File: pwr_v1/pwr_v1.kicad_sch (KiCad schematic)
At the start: 2 parts

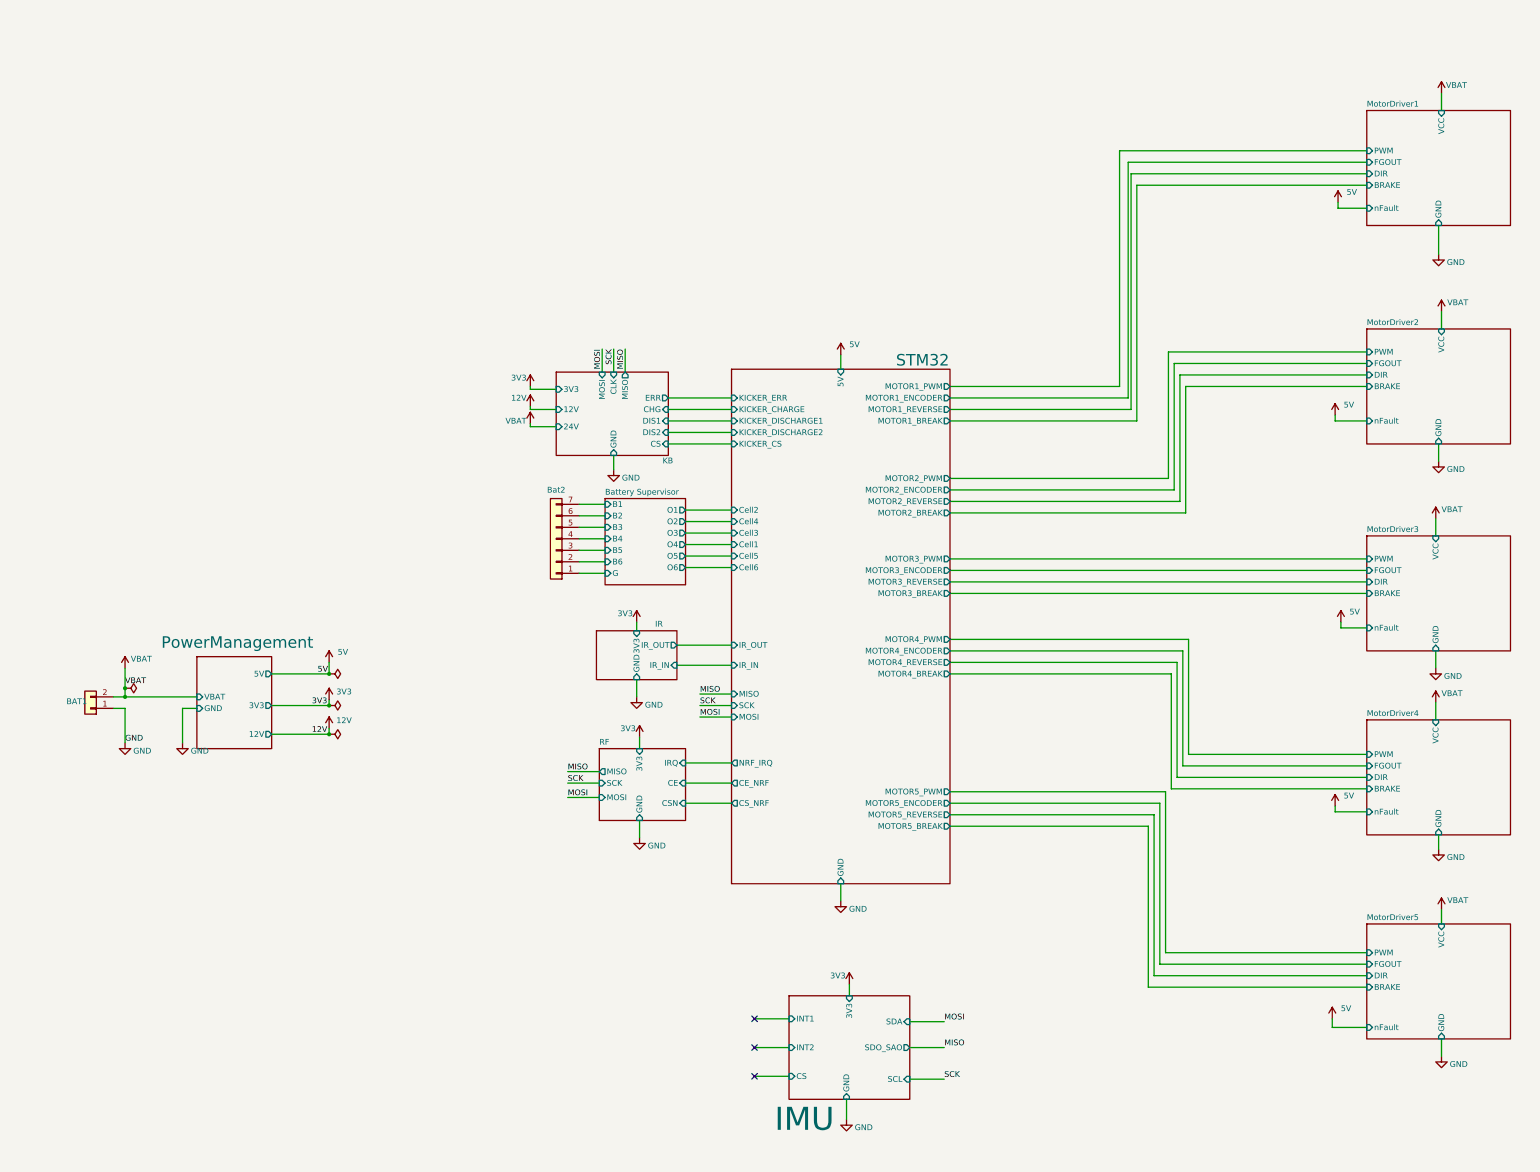
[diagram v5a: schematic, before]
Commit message: Schematic and layout updated; Layout placement and routing completed
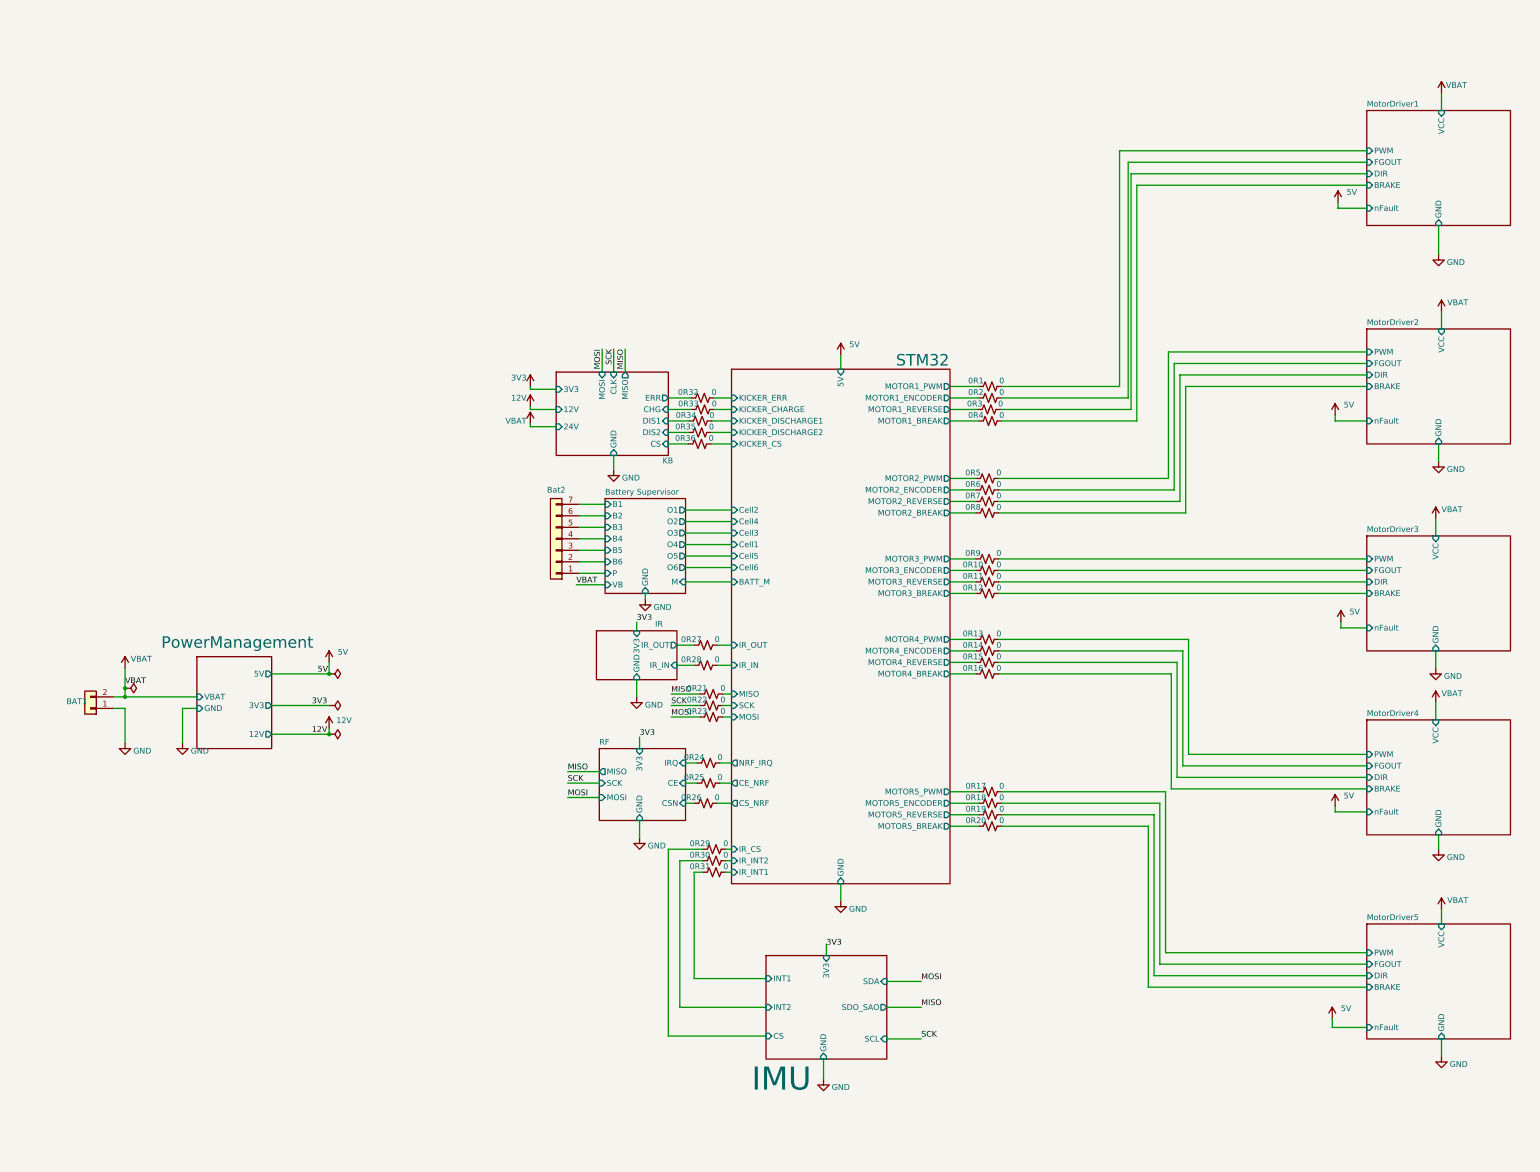
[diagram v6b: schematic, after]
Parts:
- added 0R1, 0R10, 0R11, 0R12, 0R13, 0R14, 0R15, 0R16, 0R17, 0R18, 0R19, 0R2, 0R20, 0R21, 0R22, 0R23, 0R24, 0R25, 0R26, 0R27, 0R28, 0R29, 0R3, 0R30, 0R31, 0R32, 0R33, 0R34, 0R35, 0R36, 0R4, 0R5, 0R6, 0R7, 0R8, 0R9: 0, Resistor_SMD:R_0603_1608Metric, symbol Device:R_Small_US
- Bat2: footprint (none) -> B7B_XH_A:JST_B7B-XH-A
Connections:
- net IMU/CS: now also 0R29.1
- net IMU/INT1: now also 0R31.1
- net IMU/INT2: now also 0R30.1
- net IR/IR_IN: now also 0R28.1
- net IR/IR_OUT: now also 0R27.1
- net KB/CHG: now also 0R33.1
- net KB/CS: now also 0R36.1
- net KB/DIS1: now also 0R34.1
- net KB/DIS2: now also 0R35.1
- net KB/ERR: now also 0R32.1
- net MISO: now also 0R21.1
- net MOSI: now also 0R23.1
- net MotorDriver1/BRAKE: now also 0R4.2
- net MotorDriver1/DIR: now also 0R3.2
- net MotorDriver1/FGOUT: now also 0R2.2
- net MotorDriver1/PWM: now also 0R1.2
- net MotorDriver2/BRAKE: now also 0R8.2
- net MotorDriver2/DIR: now also 0R7.2
- net MotorDriver2/FGOUT: now also 0R6.2
- net MotorDriver2/PWM: now also 0R5.2
- net MotorDriver3/BRAKE: now also 0R12.2
- net MotorDriver3/DIR: now also 0R11.2
- net MotorDriver3/FGOUT: now also 0R10.2
- net MotorDriver3/PWM: now also 0R9.2
- net MotorDriver4/BRAKE: now also 0R16.2
- net MotorDriver4/DIR: now also 0R15.2
- net MotorDriver4/FGOUT: now also 0R14.2
- net MotorDriver4/PWM: now also 0R13.2
- net MotorDriver5/BRAKE: now also 0R20.2
- net MotorDriver5/DIR: now also 0R19.2
- net MotorDriver5/FGOUT: now also 0R18.2
- net MotorDriver5/PWM: now also 0R17.2
- net RF/CE: now also 0R25.1
- net RF/CSN: now also 0R26.1
- net RF/IRQ: now also 0R24.1
- net SCK: now also 0R22.1
- net Battery Supervisor/G renamed Battery Supervisor/P
- new net STM32/CE_NRF: 0R25.2
- new net STM32/CS_NRF: 0R26.2
- new net STM32/IR_CS: 0R29.2
- new net STM32/IR_IN: 0R28.2
- new net STM32/IR_INT1: 0R31.2
- new net STM32/IR_INT2: 0R30.2
- new net STM32/IR_OUT: 0R27.2
- new net STM32/KICKER_CHARGE: 0R33.2
- new net STM32/KICKER_CS: 0R36.2
- new net STM32/KICKER_DISCHARGE1: 0R34.2
- new net STM32/KICKER_DISCHARGE2: 0R35.2
- new net STM32/KICKER_ERR: 0R32.2
- new net STM32/MISO: 0R21.2
- new net STM32/MOSI: 0R23.2
- new net STM32/MOTOR1_BREAK: 0R4.1
- new net STM32/MOTOR1_ENCODER: 0R2.1
- new net STM32/MOTOR1_PWM: 0R1.1
- new net STM32/MOTOR1_REVERSE: 0R3.1
- new net STM32/MOTOR2_BREAK: 0R8.1
- new net STM32/MOTOR2_ENCODER: 0R6.1
- new net STM32/MOTOR2_PWM: 0R5.1
- new net STM32/MOTOR2_REVERSE: 0R7.1
- new net STM32/MOTOR3_BREAK: 0R12.1
- new net STM32/MOTOR3_ENCODER: 0R10.1
- new net STM32/MOTOR3_PWM: 0R9.1
- new net STM32/MOTOR3_REVERSE: 0R11.1
- new net STM32/MOTOR4_BREAK: 0R16.1
- new net STM32/MOTOR4_ENCODER: 0R14.1
- new net STM32/MOTOR4_PWM: 0R13.1
- new net STM32/MOTOR4_REVERSE: 0R15.1
- new net STM32/MOTOR5_BREAK: 0R20.1
- new net STM32/MOTOR5_ENCODER: 0R18.1
- new net STM32/MOTOR5_PWM: 0R17.1
- new net STM32/MOTOR5_REVERSE: 0R19.1
- new net STM32/NRF_IRQ: 0R24.2
- new net STM32/SCK: 0R22.2
- no-connect marks 3 -> 0
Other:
- sheet Battery Supervisor ports: added GND, M, P, VB; removed G
- sheet STM32 ports: added BATT_M, IR_CS, IR_INT1, IR_INT2; removed none

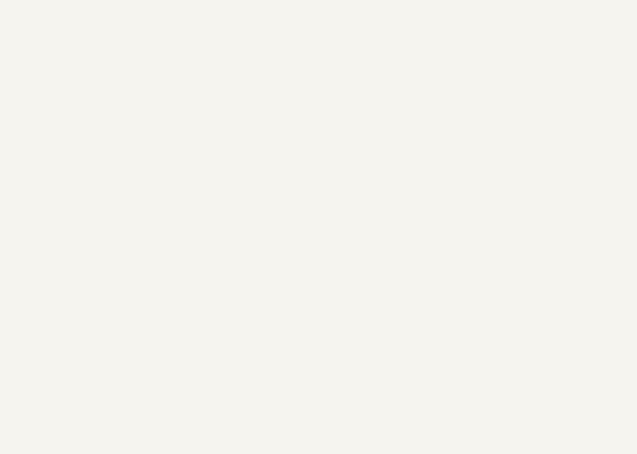
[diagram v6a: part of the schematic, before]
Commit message: Sch: Mechanical comp added; Lay: SIlkscreen aligned, trace widths updated to atleast 12 mils.
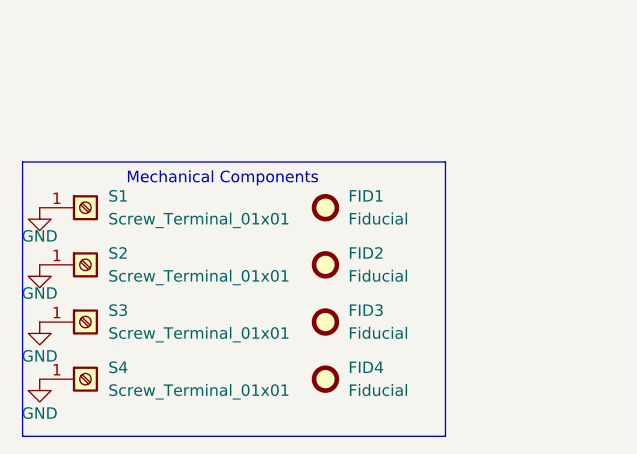
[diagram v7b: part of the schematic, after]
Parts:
- added FID1, FID2, FID3, FID4: Fiducial, Fiducial:Fiducial_1mm_Mask2mm, symbol Mechanical:Fiducial
- added S1, S2, S3, S4: Screw_Terminal_01x01, TerminalBlock_MetzConnect:TerminalBlock_MetzConnect_360271_1x01_Horizontal_ScrewM3.0_Boxed, symbol Connector:Screw_Terminal_01x01
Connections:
- net GND: now also S1.1 (Pin_1), S2.1 (Pin_1), S3.1 (Pin_1), S4.1 (Pin_1)
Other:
- note added: "Mechanical Components"

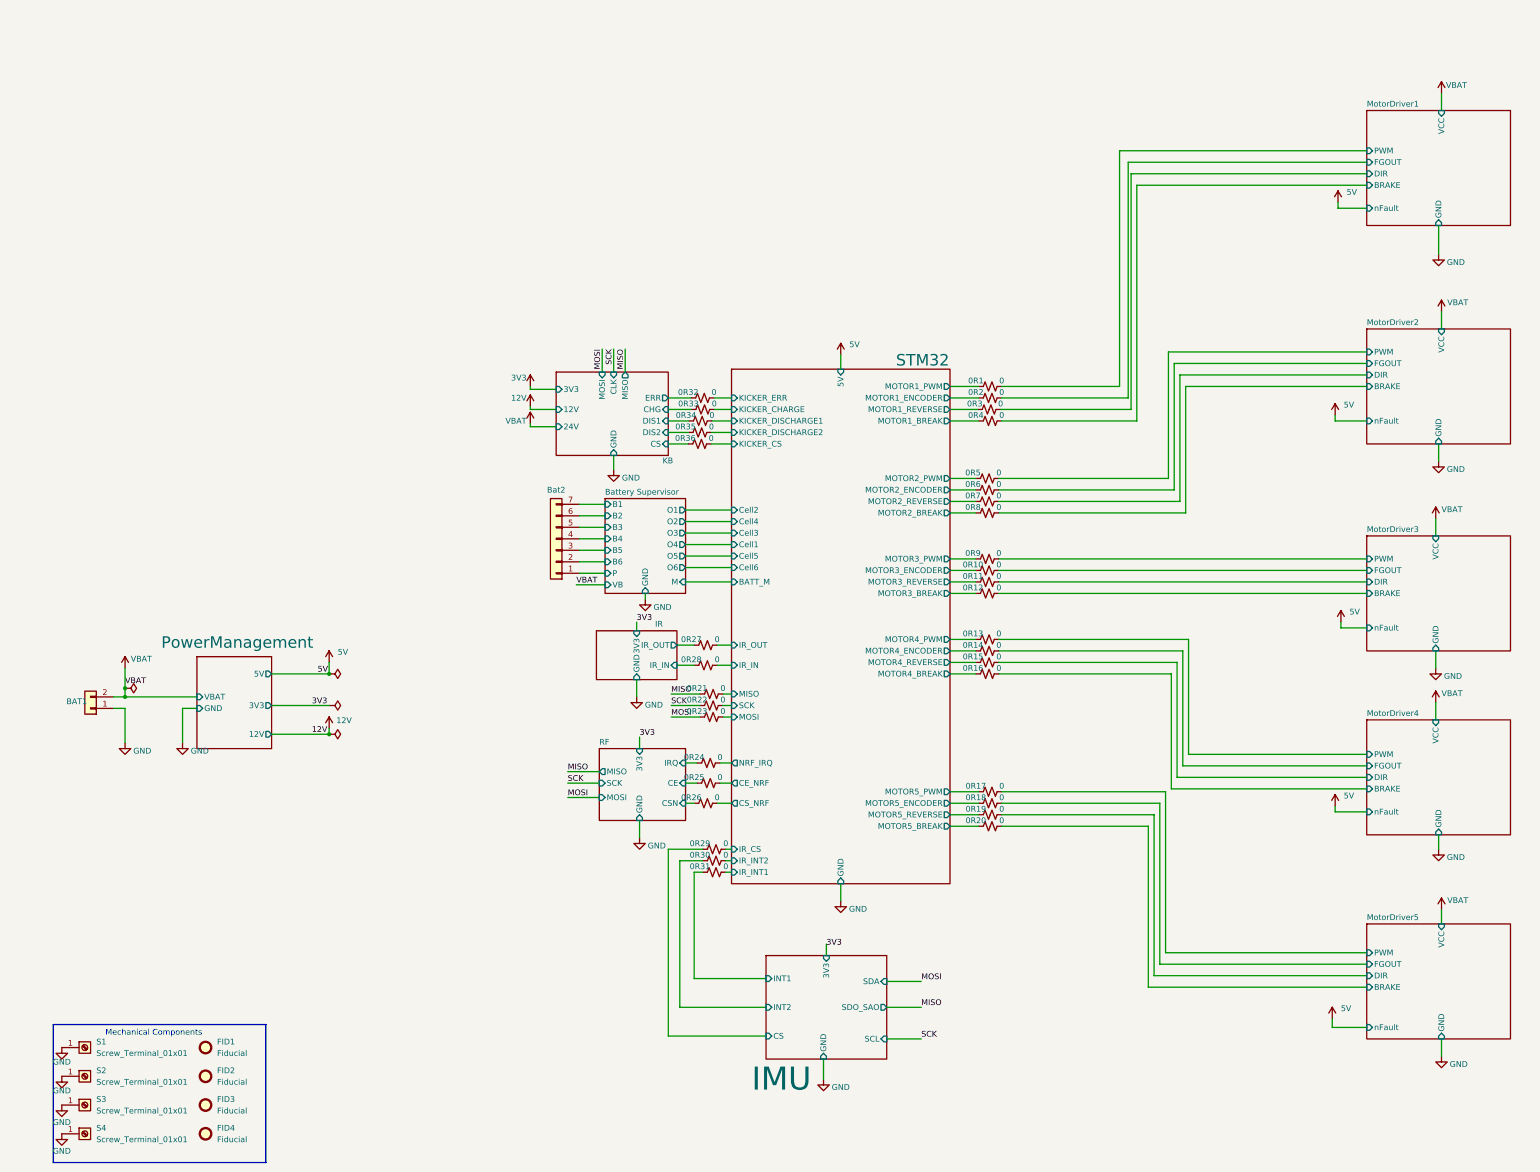
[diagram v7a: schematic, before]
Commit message: Sch: 0ohm res added to SPI pins, MD footprints updated; Lay: Silkscreen aligned, logo added, DRC
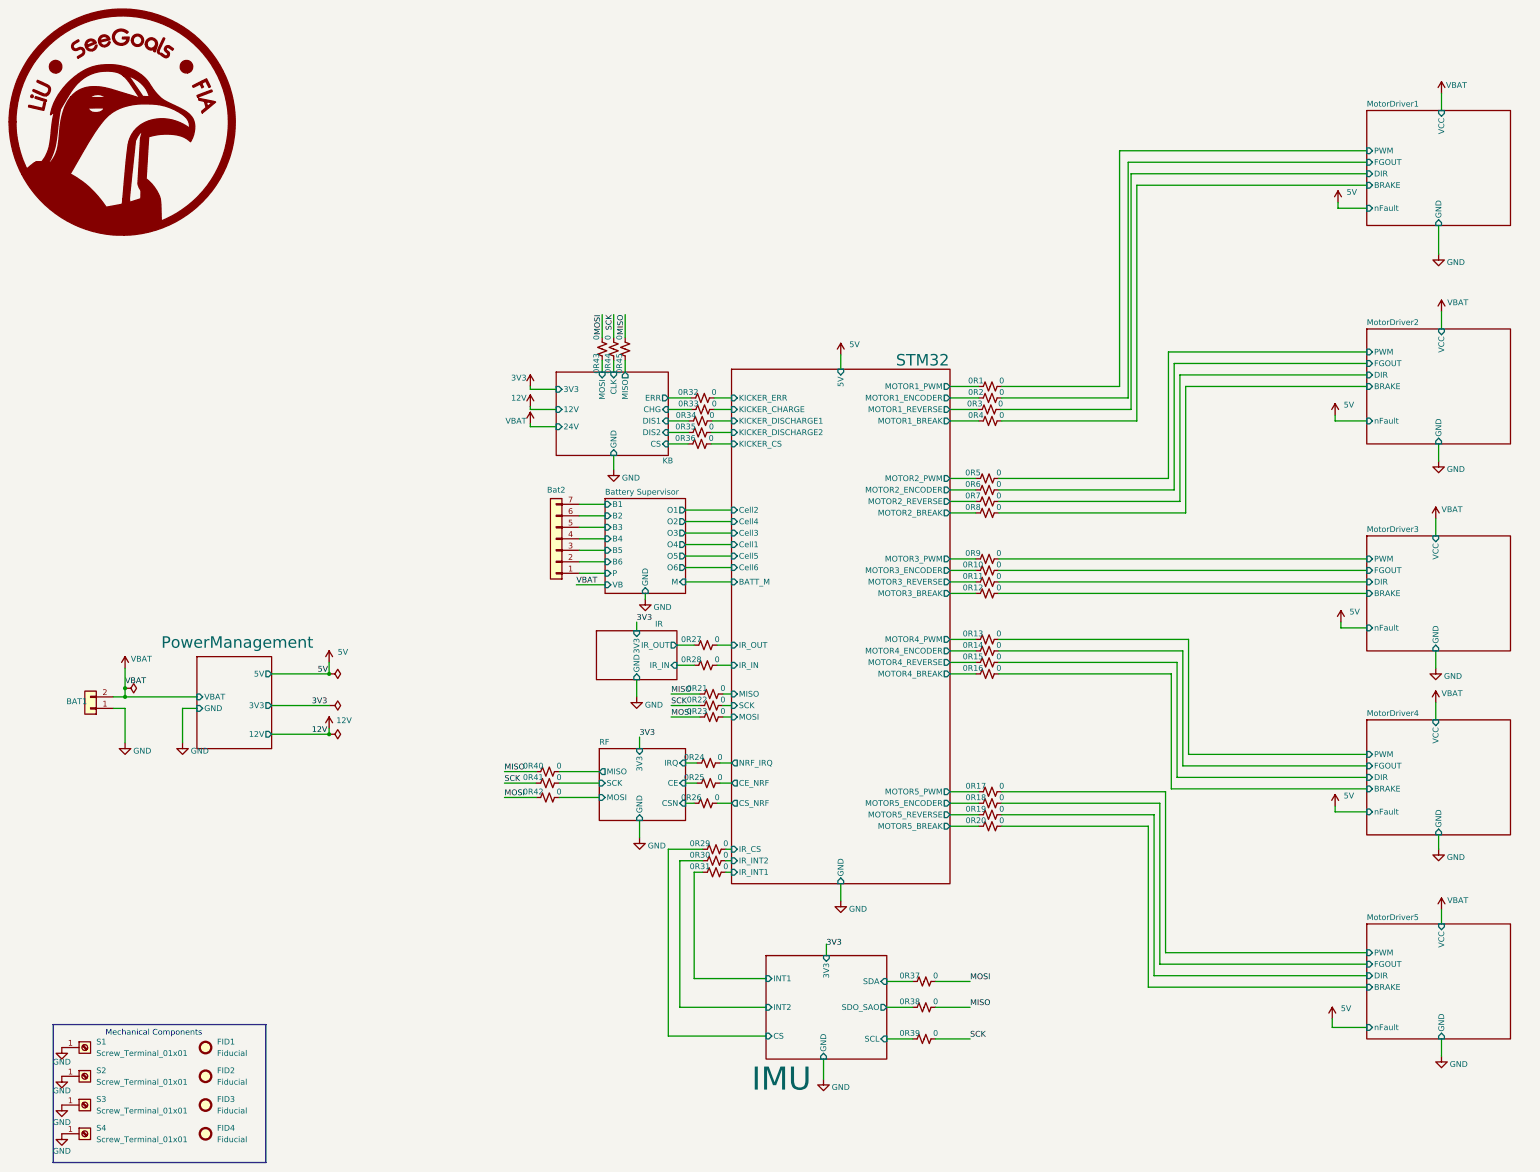
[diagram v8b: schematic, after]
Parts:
- added 0R37, 0R38, 0R39, 0R40, 0R41, 0R42, 0R43, 0R44, 0R45: 0, Resistor_SMD:R_0603_1608Metric, symbol Device:R_Small_US
- S1, S2, S3, S4: now left out of the parts list
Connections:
- net MISO: now also 0R38.2, 0R40.1, 0R45.2
- net MOSI: now also 0R37.2, 0R42.1, 0R43.2
- net SCK: now also 0R39.2, 0R41.1, 0R44.2
- new net IMU/SCL: 0R39.1
- new net IMU/SDA: 0R37.1
- new net IMU/SDO_SAO: 0R38.1
- new net KB/CLK: 0R44.1
- new net KB/MISO: 0R45.1
- new net KB/MOSI: 0R43.1
- new net RF/MISO: 0R40.2
- new net RF/MOSI: 0R42.2
- new net RF/SCK: 0R41.2
